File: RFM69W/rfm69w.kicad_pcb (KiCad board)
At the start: 2 copper layers, 27.9 x 33 mm, 9 parts, among them J1 Conn1, J2 Conn2, J3 U.FL / IPEX, J4 SMA, U1 RFM69W

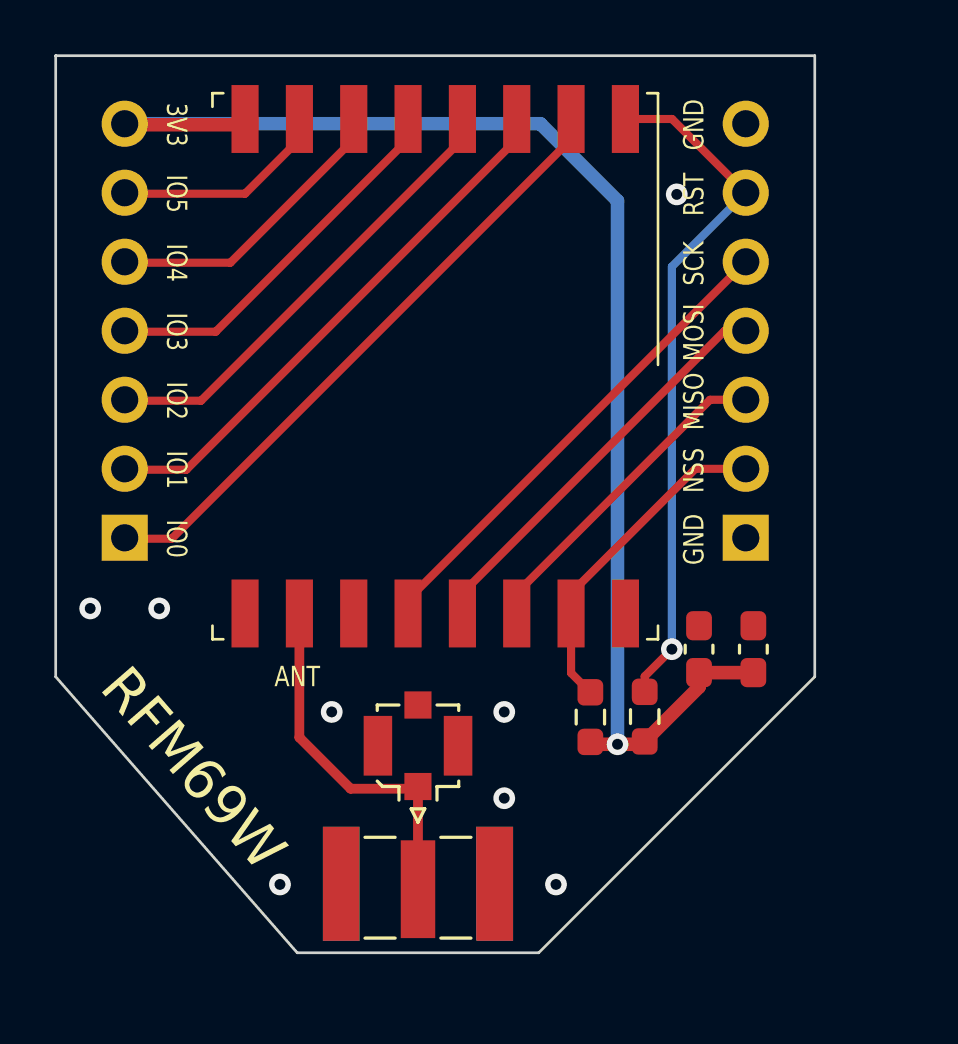
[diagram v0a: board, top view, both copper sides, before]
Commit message: Updated the RFM69W and RFM95W/RFM96W board layouts.
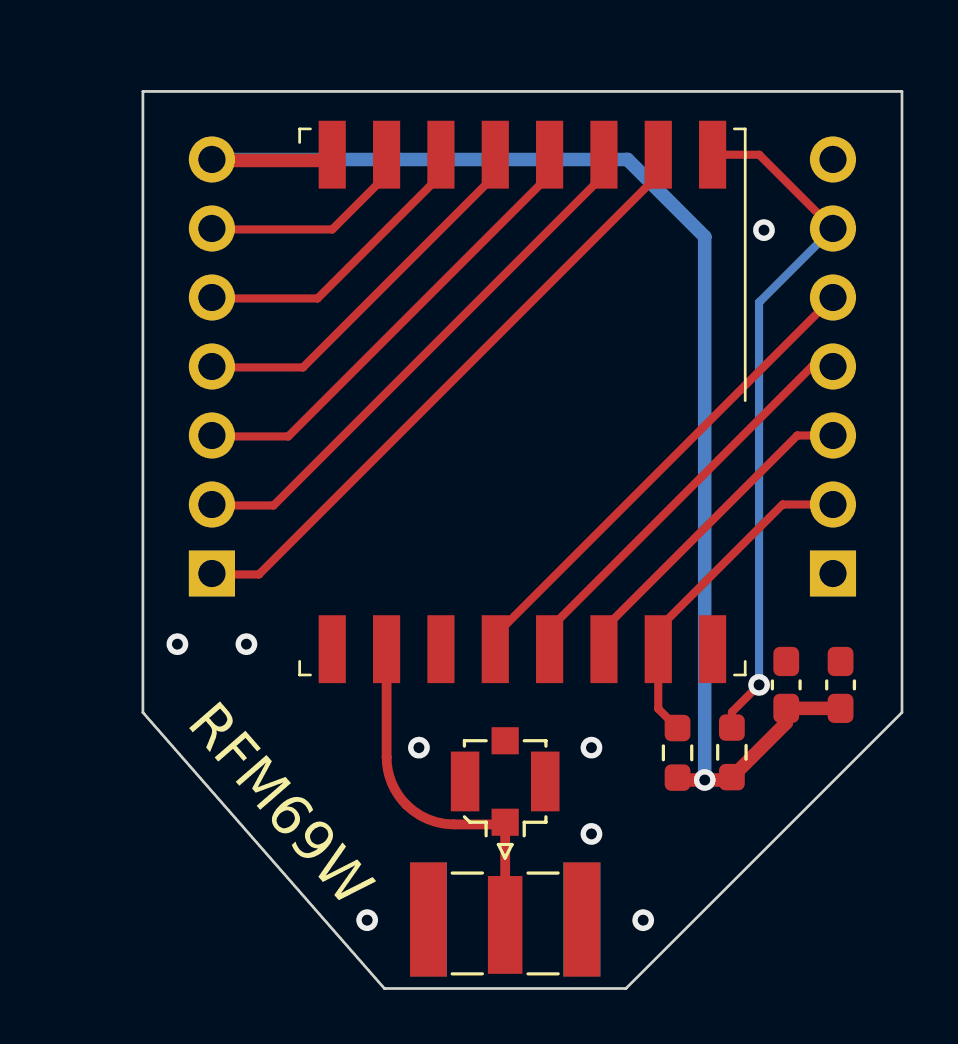
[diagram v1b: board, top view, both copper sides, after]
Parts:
- moved J2 3.47 mm to (112.4, 62.2)
- moved J1 3.47 mm to (89.6, 62.2)
- moved C1 3.47 mm to (112.7, 66.3)
- moved C2 3.47 mm to (110.7, 66.3)
- moved J3 3.47 mm to (100.4, 69.9)
- moved J4 3.47 mm to (100.4, 75.0)
- moved R1 3.47 mm to (106.7, 68.8)
- moved R2 3.47 mm to (108.7, 68.8)
- moved U1 3.47 mm to (101.0, 55.9)
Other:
- board text added: "0"
- board text added: "1"
- board text added: "2"
- board text added: "3"
- board text added: "4"
- board text added: "5"
- board text added: "DIO"
- board text added: "Rev 1 2248"
- board text removed: "ANT"
- board text removed: "IO0"
- board text removed: "IO1"
- board text removed: "IO2"
- board text removed: "IO3"
- board text removed: "IO4"
- board text removed: "IO5"
- board text removed: "Rev1"
